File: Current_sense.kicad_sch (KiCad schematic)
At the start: 5 parts, among them U33 INA180A4

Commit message: pcb is in progress, finishing H-bridge layout
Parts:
- R64: footprint Resistor_SMD:R_2512_6332Metric -> Resistor_SMD:R_2512_6332Metric_Pad1.40x3.35mm_HandSolder
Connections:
- net INA_OUT: now reaches R65.1, U33.1 (OUT)
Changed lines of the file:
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@@
     (effects (font (size 1.27 1.27)) (justify left bottom))
+  )
+  (label "INA_OUT" (at 139.7 82.55 0)
+    (effects (font (size 0.7 0.7)) (justify left bottom))
   )
   (hierarchical_label "OUT-" (shape output) (at 104.14 90.17 270)
@@
       (effects (font (size 1.27 1.27)) (justify left))
     )
-    (property "Footprint" "Resistor_SMD:R_2512_6332Metric" (id 2) (at 102.362 82.55 90)
+    (property "Footprint" "Resistor_SMD:R_2512_6332Metric_Pad1.40x3.35mm_HandSolder" (id 2) (at 102.362 82.55 90)
       (effects (font (size 1.27 1.27)) hide)
     )

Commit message: start design power input
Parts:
- added R111, R112, R113: 8mR, Resistor_SMD:R_2512_6332Metric_Pad1.40x3.35mm_HandSolder, symbol Device:R
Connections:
- net IN+: now also R111.1
- net OUT-: now also R112.2, R113.2; no longer R64.2
- new net: R111.2, R112.1
- new net: R113.1, R64.2
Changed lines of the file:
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@@
   (junction (at 104.14 77.47) (diameter 0) (color 0 0 0 0)
   )
-  (junction (at 104.14 87.63) (diameter 0) (color 0 0 0 0)
+  (junction (at 104.14 95.25) (diameter 0) (color 0 0 0 0)
+  )
+  (junction (at 104.14 96.52) (diameter 0) (color 0 0 0 0)
   )
   (wire (pts (xy 110.49 77.47) (xy 110.49 78.74))
     (stroke (width 0) (type default) (color 0 0 0 0))
   )
-  (wire (pts (xy 104.14 87.63) (xy 110.49 87.63))
-    (stroke (width 0) (type default) (color 0 0 0 0))
-  )
   (wire (pts (xy 162.56 82.55) (xy 165.1 82.55))
     (stroke (width 0) (type default) (color 0 0 0 0))
   )
-  (wire (pts (xy 104.14 87.63) (xy 104.14 90.17))
-    (stroke (width 0) (type default) (color 0 0 0 0))
-  )
   (wire (pts (xy 104.14 78.74) (xy 104.14 77.47))
     (stroke (width 0) (type default) (color 0 0 0 0))
@@
     (stroke (width 0) (type default) (color 0 0 0 0))
   )
+  (wire (pts (xy 110.49 95.25) (xy 104.14 95.25))
+    (stroke (width 0) (type default) (color 0 0 0 0))
+  )
+  (wire (pts (xy 100.33 77.47) (xy 104.14 77.47))
+    (stroke (width 0) (type default) (color 0 0 0 0))
+  )
   (wire (pts (xy 104.14 74.93) (xy 104.14 77.47))
     (stroke (width 0) (type default) (color 0 0 0 0))
   )
-  (wire (pts (xy 104.14 86.36) (xy 104.14 87.63))
+  (wire (pts (xy 104.14 96.52) (xy 104.14 97.79))
+    (stroke (width 0) (type default) (color 0 0 0 0))
+  )
+  (wire (pts (xy 100.33 96.52) (xy 104.14 96.52))
+    (stroke (width 0) (type default) (color 0 0 0 0))
+  )
+  (wire (pts (xy 100.33 78.74) (xy 100.33 77.47))
     (stroke (width 0) (type default) (color 0 0 0 0))
   )
@@
     (stroke (width 0) (type default) (color 0 0 0 0))
   )
-  (wire (pts (xy 110.49 87.63) (xy 110.49 86.36))
+  (wire (pts (xy 104.14 93.98) (xy 104.14 95.25))
+    (stroke (width 0) (type default) (color 0 0 0 0))
+  )
+  (wire (pts (xy 110.49 86.36) (xy 110.49 95.25))
     (stroke (width 0) (type default) (color 0 0 0 0))
   )
@@
     (stroke (width 0) (type default) (color 0 0 0 0))
   )
+  (wire (pts (xy 104.14 95.25) (xy 104.14 96.52))
+    (stroke (width 0) (type default) (color 0 0 0 0))
+  )
   (wire (pts (xy 133.35 82.55) (xy 152.4 82.55))
     (stroke (width 0) (type default) (color 0 0 0 0))
@@
   )
   (wire (pts (xy 110.49 86.36) (xy 113.03 86.36))
+    (stroke (width 0) (type default) (color 0 0 0 0))
+  )
+  (wire (pts (xy 100.33 93.98) (xy 100.33 96.52))
     (stroke (width 0) (type default) (color 0 0 0 0))
   )
@@
     (effects (font (size 0.7 0.7)) (justify left bottom))
   )
-  (hierarchical_label "OUT-" (shape output) (at 104.14 90.17 270)
+  (hierarchical_label "OUT-" (shape output) (at 104.14 97.79 270)
     (effects (font (size 1.27 1.27)) (justify right))
   )
@@
     )
     (property "Datasheet" "~" (id 3) (at 162.56 92.71 0)
+      (effects (font (size 1.27 1.27)) hide)
+    )
+    (pin "1")
+    (pin "2")
+  )
+  (symbol (lib_id "Device:R") (at 100.33 90.17 0) (unit 1)
+    (in_bom yes) (on_board yes)
+    (property "Reference" "R112" (id 0) (at 95.25 88.9 0)
+      (effects (font (size 1.27 1.27)) (justify left))
+    )
+    (property "Value" "8mR" (id 1) (at 93.98 91.44 0)
+      (effects (font (size 1.27 1.27)) (justify left))
+    )
+    (property "Footprint" "Resistor_SMD:R_2512_6332Metric_Pad1.40x3.35mm_HandSolder" (id 2) (at 98.552 90.17 90)
+      (effects (font (size 1.27 1.27)) hide)
+    )
+    (property "Datasheet" "~" (id 3) (at 100.33 90.17 0)
       (effects (font (size 1.27 1.27)) hide)
     )
@@
     (pin "1")
   )
+  (symbol (lib_id "Device:R") (at 104.14 90.17 0) (unit 1)
+    (in_bom yes) (on_board yes) (fields_autoplaced)
+    (property "Reference" "R113" (id 0) (at 106.68 88.8999 0)
+      (effects (font (size 1.27 1.27)) (justify left))
+    )
+    (property "Value" "8mR" (id 1) (at 106.68 91.4399 0)
+      (effects (font (size 1.27 1.27)) (justify left))
+    )
+    (property "Footprint" "Resistor_SMD:R_2512_6332Metric_Pad1.40x3.35mm_HandSolder" (id 2) (at 102.362 90.17 90)
+      (effects (font (size 1.27 1.27)) hide)
+    )
+    (property "Datasheet" "~" (id 3) (at 104.14 90.17 0)
+      (effects (font (size 1.27 1.27)) hide)
+    )
+    (pin "1")
+    (pin "2")
+  )
   (symbol (lib_id "Device:R") (at 156.21 82.55 90) (unit 1)
     (in_bom yes) (on_board yes) (fields_autoplaced)
@@
     (pin "1")
   )
+  (symbol (lib_id "Device:R") (at 100.33 82.55 0) (unit 1)
+    (in_bom yes) (on_board yes)
+    (property "Reference" "R111" (id 0) (at 95.25 81.28 0)
+      (effects (font (size 1.27 1.27)) (justify left))
+    )
+    (property "Value" "8mR" (id 1) (at 93.98 83.82 0)
+      (effects (font (size 1.27 1.27)) (justify left))
+    )
+    (property "Footprint" "Resistor_SMD:R_2512_6332Metric_Pad1.40x3.35mm_HandSolder" (id 2) (at 98.552 82.55 90)
+      (effects (font (size 1.27 1.27)) hide)
+    )
+    (property "Datasheet" "~" (id 3) (at 100.33 82.55 0)
+      (effects (font (size 1.27 1.27)) hide)
+    )
+    (pin "1")
+    (pin "2")
+  )
   (symbol (lib_id "Device:C") (at 135.89 92.71 0) (unit 1)

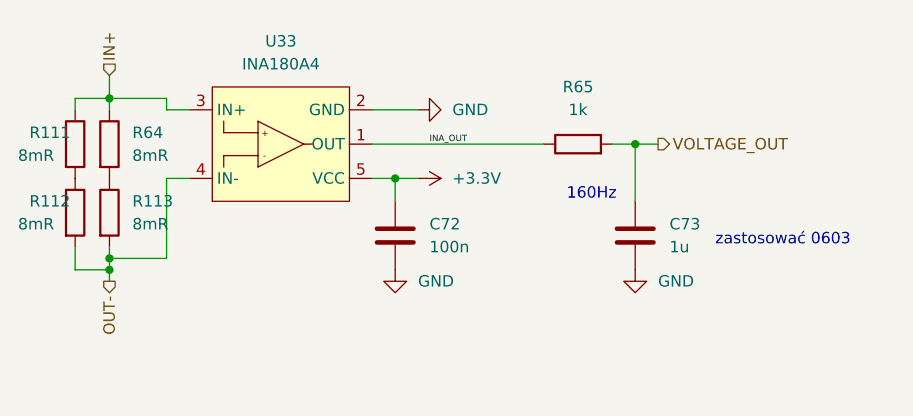
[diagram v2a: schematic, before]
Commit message: power part designed
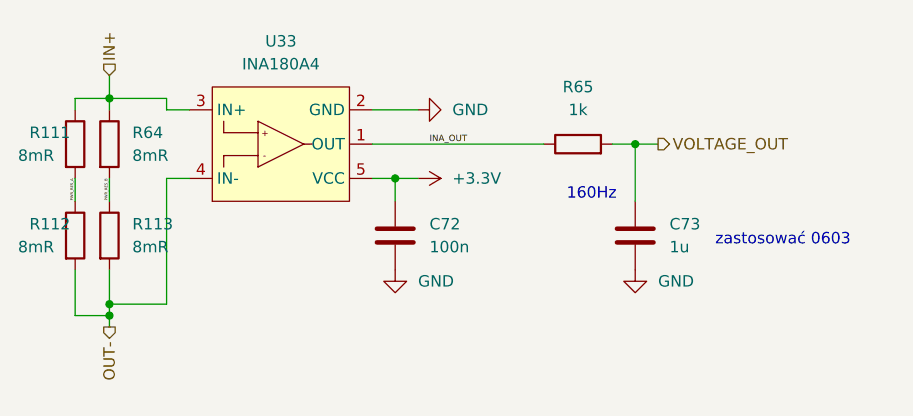
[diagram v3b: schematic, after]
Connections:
- net PWR_RES_A: now reaches R111.2, R112.1
- net PWR_RES_B: now reaches R113.1, R64.2
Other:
- moved on the sheet: R112, R113
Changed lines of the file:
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@@
   (junction (at 104.14 77.47) (diameter 0) (color 0 0 0 0)
   )
-  (junction (at 104.14 95.25) (diameter 0) (color 0 0 0 0)
-  )
-  (junction (at 104.14 96.52) (diameter 0) (color 0 0 0 0)
+  (junction (at 104.14 100.33) (diameter 0) (color 0 0 0 0)
+  )
+  (junction (at 104.14 101.6) (diameter 0) (color 0 0 0 0)
   )
   (wire (pts (xy 110.49 77.47) (xy 110.49 78.74))
@@
     (stroke (width 0) (type default) (color 0 0 0 0))
   )
+  (wire (pts (xy 104.14 96.52) (xy 104.14 100.33))
+    (stroke (width 0) (type default) (color 0 0 0 0))
+  )
   (wire (pts (xy 104.14 78.74) (xy 104.14 77.47))
     (stroke (width 0) (type default) (color 0 0 0 0))
@@
     (stroke (width 0) (type default) (color 0 0 0 0))
   )
-  (wire (pts (xy 110.49 95.25) (xy 104.14 95.25))
+  (wire (pts (xy 110.49 100.33) (xy 104.14 100.33))
+    (stroke (width 0) (type default) (color 0 0 0 0))
+  )
+  (wire (pts (xy 104.14 88.9) (xy 104.14 86.36))
     (stroke (width 0) (type default) (color 0 0 0 0))
   )
@@
     (stroke (width 0) (type default) (color 0 0 0 0))
   )
-  (wire (pts (xy 104.14 96.52) (xy 104.14 97.79))
-    (stroke (width 0) (type default) (color 0 0 0 0))
-  )
-  (wire (pts (xy 100.33 96.52) (xy 104.14 96.52))
+  (wire (pts (xy 110.49 86.36) (xy 110.49 100.33))
+    (stroke (width 0) (type default) (color 0 0 0 0))
+  )
+  (wire (pts (xy 104.14 101.6) (xy 104.14 102.87))
+    (stroke (width 0) (type default) (color 0 0 0 0))
+  )
+  (wire (pts (xy 100.33 101.6) (xy 104.14 101.6))
     (stroke (width 0) (type default) (color 0 0 0 0))
   )
@@
     (stroke (width 0) (type default) (color 0 0 0 0))
   )
-  (wire (pts (xy 104.14 93.98) (xy 104.14 95.25))
-    (stroke (width 0) (type default) (color 0 0 0 0))
-  )
-  (wire (pts (xy 110.49 86.36) (xy 110.49 95.25))
+  (wire (pts (xy 113.03 86.36) (xy 110.49 86.36))
     (stroke (width 0) (type default) (color 0 0 0 0))
   )
@@
     (stroke (width 0) (type default) (color 0 0 0 0))
   )
-  (wire (pts (xy 104.14 95.25) (xy 104.14 96.52))
+  (wire (pts (xy 104.14 100.33) (xy 104.14 101.6))
     (stroke (width 0) (type default) (color 0 0 0 0))
   )
@@
     (stroke (width 0) (type default) (color 0 0 0 0))
   )
+  (wire (pts (xy 100.33 96.52) (xy 100.33 101.6))
+    (stroke (width 0) (type default) (color 0 0 0 0))
+  )
   (wire (pts (xy 104.14 77.47) (xy 110.49 77.47))
     (stroke (width 0) (type default) (color 0 0 0 0))
@@
     (stroke (width 0) (type default) (color 0 0 0 0))
   )
-  (wire (pts (xy 110.49 86.36) (xy 113.03 86.36))
-    (stroke (width 0) (type default) (color 0 0 0 0))
-  )
-  (wire (pts (xy 100.33 93.98) (xy 100.33 96.52))
-    (stroke (width 0) (type default) (color 0 0 0 0))
-  )
   (wire (pts (xy 135.89 86.36) (xy 133.35 86.36))
+    (stroke (width 0) (type default) (color 0 0 0 0))
+  )
+  (wire (pts (xy 100.33 88.9) (xy 100.33 86.36))
     (stroke (width 0) (type default) (color 0 0 0 0))
   )
@@
     (effects (font (size 1.27 1.27)) (justify left bottom))
   )
+  (label "PWR_RES_B" (at 104.14 86.36 270)
+    (effects (font (size 0.3 0.3)) (justify right bottom))
+  )
   (label "INA_OUT" (at 139.7 82.55 0)
     (effects (font (size 0.7 0.7)) (justify left bottom))
   )
-  (hierarchical_label "OUT-" (shape output) (at 104.14 97.79 270)
+  (label "PWR_RES_A" (at 100.33 86.36 270)
+    (effects (font (size 0.3 0.3)) (justify right bottom))
+  )
+  (hierarchical_label "OUT-" (shape output) (at 104.14 102.87 270)
     (effects (font (size 1.27 1.27)) (justify right))
   )
@@
     (pin "2")
   )
-  (symbol (lib_id "Device:R") (at 100.33 90.17 0) (unit 1)
+  (symbol (lib_id "Device:R") (at 100.33 92.71 0) (unit 1)
     (in_bom yes) (on_board yes)
-    (property "Reference" "R112" (id 0) (at 95.25 88.9 0)
-      (effects (font (size 1.27 1.27)) (justify left))
-    )
-    (property "Value" "8mR" (id 1) (at 93.98 91.44 0)
-      (effects (font (size 1.27 1.27)) (justify left))
-    )
-    (property "Footprint" "Resistor_SMD:R_2512_6332Metric_Pad1.40x3.35mm_HandSolder" (id 2) (at 98.552 90.17 90)
-      (effects (font (size 1.27 1.27)) hide)
-    )
-    (property "Datasheet" "~" (id 3) (at 100.33 90.17 0)
+    (property "Reference" "R112" (id 0) (at 95.25 91.44 0)
+      (effects (font (size 1.27 1.27)) (justify left))
+    )
+    (property "Value" "8mR" (id 1) (at 93.98 93.98 0)
+      (effects (font (size 1.27 1.27)) (justify left))
+    )
+    (property "Footprint" "Resistor_SMD:R_2512_6332Metric_Pad1.40x3.35mm_HandSolder" (id 2) (at 98.552 92.71 90)
+      (effects (font (size 1.27 1.27)) hide)
+    )
+    (property "Datasheet" "~" (id 3) (at 100.33 92.71 0)
       (effects (font (size 1.27 1.27)) hide)
     )
@@
     (pin "1")
   )
-  (symbol (lib_id "Device:R") (at 104.14 90.17 0) (unit 1)
-    (in_bom yes) (on_board yes) (fields_autoplaced)
-    (property "Reference" "R113" (id 0) (at 106.68 88.8999 0)
-      (effects (font (size 1.27 1.27)) (justify left))
-    )
-    (property "Value" "8mR" (id 1) (at 106.68 91.4399 0)
-      (effects (font (size 1.27 1.27)) (justify left))
-    )
-    (property "Footprint" "Resistor_SMD:R_2512_6332Metric_Pad1.40x3.35mm_HandSolder" (id 2) (at 102.362 90.17 90)
-      (effects (font (size 1.27 1.27)) hide)
-    )
-    (property "Datasheet" "~" (id 3) (at 104.14 90.17 0)
-      (effects (font (size 1.27 1.27)) hide)
-    )
+  (symbol (lib_id "Device:R") (at 104.14 92.71 0) (unit 1)
+    (in_bom yes) (on_board yes) (fields_autoplaced)
+    (property "Reference" "R113" (id 0) (at 106.68 91.4399 0)
+      (effects (font (size 1.27 1.27)) (justify left))
+    )
+    (property "Value" "8mR" (id 1) (at 106.68 93.9799 0)
+      (effects (font (size 1.27 1.27)) (justify left))
+    )
+    (property "Footprint" "Resistor_SMD:R_2512_6332Metric_Pad1.40x3.35mm_HandSolder" (id 2) (at 102.362 92.71 90)
+      (effects (font (size 1.27 1.27)) hide)
+    )
+    (property "Datasheet" "~" (id 3) (at 104.14 92.71 0)
+      (effects (font (size 1.27 1.27)) hide)
+    )

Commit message: ADC resistors and outputs added
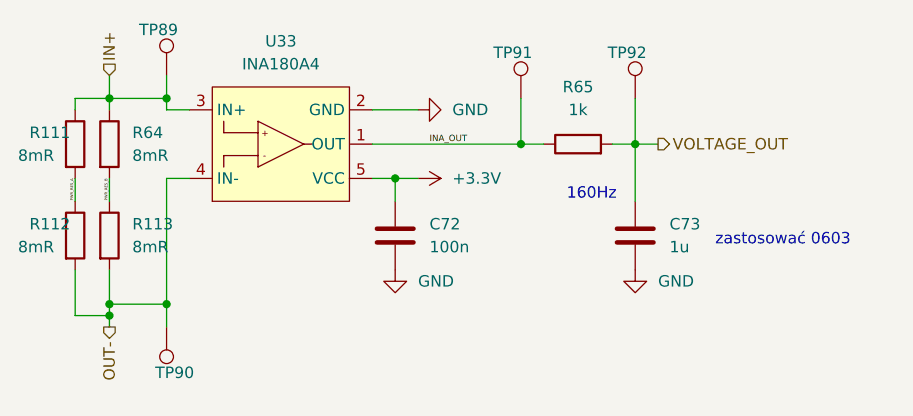
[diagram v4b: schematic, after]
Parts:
- added TP89, TP90, TP91, TP92: TestPoint, TestPoint:TestPoint_THTPad_1.0x1.0mm_Drill0.5mm, symbol Connector:TestPoint
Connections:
- net IN+: now also TP89.1
- net INA_OUT: now also TP91.1
- net OUT-: now also TP90.1
- net VOLTAGE_OUT: now also TP92.1
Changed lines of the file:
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@@
   (junction (at 135.89 86.36) (diameter 0) (color 0 0 0 0)
   )
+  (junction (at 149.86 82.55) (diameter 0) (color 0 0 0 0)
+  )
   (junction (at 104.14 77.47) (diameter 0) (color 0 0 0 0)
   )
+  (junction (at 110.49 77.47) (diameter 0) (color 0 0 0 0)
+  )
+  (junction (at 110.49 100.33) (diameter 0) (color 0 0 0 0)
+  )
   (junction (at 104.14 100.33) (diameter 0) (color 0 0 0 0)
   )
@@
     (stroke (width 0) (type default) (color 0 0 0 0))
   )
+  (wire (pts (xy 149.86 77.47) (xy 149.86 82.55))
+    (stroke (width 0) (type default) (color 0 0 0 0))
+  )
   (wire (pts (xy 162.56 82.55) (xy 165.1 82.55))
     (stroke (width 0) (type default) (color 0 0 0 0))
@@
     (stroke (width 0) (type default) (color 0 0 0 0))
   )
+  (wire (pts (xy 110.49 100.33) (xy 110.49 102.87))
+    (stroke (width 0) (type default) (color 0 0 0 0))
+  )
   (wire (pts (xy 135.89 86.36) (xy 135.89 88.9))
     (stroke (width 0) (type default) (color 0 0 0 0))
@@
     (stroke (width 0) (type default) (color 0 0 0 0))
   )
+  (wire (pts (xy 110.49 74.93) (xy 110.49 77.47))
+    (stroke (width 0) (type default) (color 0 0 0 0))
+  )
   (wire (pts (xy 100.33 101.6) (xy 104.14 101.6))
     (stroke (width 0) (type default) (color 0 0 0 0))
@@
     (stroke (width 0) (type default) (color 0 0 0 0))
   )
-  (wire (pts (xy 133.35 82.55) (xy 152.4 82.55))
+  (wire (pts (xy 133.35 82.55) (xy 149.86 82.55))
+    (stroke (width 0) (type default) (color 0 0 0 0))
+  )
+  (wire (pts (xy 149.86 82.55) (xy 152.4 82.55))
     (stroke (width 0) (type default) (color 0 0 0 0))
   )
@@
   )
   (wire (pts (xy 100.33 88.9) (xy 100.33 86.36))
+    (stroke (width 0) (type default) (color 0 0 0 0))
+  )
+  (wire (pts (xy 162.56 77.47) (xy 162.56 82.55))
     (stroke (width 0) (type default) (color 0 0 0 0))
   )
@@
     (pin "2")
   )
+  (symbol (lib_id "Connector:TestPoint") (at 149.86 77.47 0) (unit 1)
+    (in_bom yes) (on_board yes)
+    (property "Reference" "TP91" (id 0) (at 151.13 72.39 0)
+      (effects (font (size 1.27 1.27)) (justify right))
+    )
+    (property "Value" "TestPoint" (id 1) (at 147.32 72.8981 0)
+      (effects (font (size 1.27 1.27)) (justify right) hide)
+    )
+    (property "Footprint" "TestPoint:TestPoint_THTPad_1.0x1.0mm_Drill0.5mm" (id 2) (at 154.94 77.47 0)
+      (effects (font (size 1.27 1.27)) hide)
+    )
+    (property "Datasheet" "~" (id 3) (at 154.94 77.47 0)
+      (effects (font (size 1.27 1.27)) hide)
+    )
+    (pin "1")
+  )
   (symbol (lib_id "Device:R") (at 100.33 92.71 0) (unit 1)
     (in_bom yes) (on_board yes)
@@
     (pin "1")
     (pin "2")
+  )
+  (symbol (lib_id "Connector:TestPoint") (at 110.49 74.93 0) (unit 1)
+    (in_bom yes) (on_board yes)
+    (property "Reference" "TP89" (id 0) (at 111.76 69.85 0)
+      (effects (font (size 1.27 1.27)) (justify right))
+    )
+    (property "Value" "TestPoint" (id 1) (at 107.95 70.3581 0)
+      (effects (font (size 1.27 1.27)) (justify right) hide)
+    )
+    (property "Footprint" "TestPoint:TestPoint_THTPad_1.0x1.0mm_Drill0.5mm" (id 2) (at 115.57 74.93 0)
+      (effects (font (size 1.27 1.27)) hide)
+    )
+    (property "Datasheet" "~" (id 3) (at 115.57 74.93 0)
+      (effects (font (size 1.27 1.27)) hide)
+    )
+    (pin "1")
   )
   (symbol (lib_id "_IntegratedCircuits:INA180A4") (at 123.19 82.55 0) (mirror x) (unit 1)
@@
     (pin "2")
   )
+  (symbol (lib_id "Connector:TestPoint") (at 110.49 102.87 180) (unit 1)
+    (in_bom yes) (on_board yes)
+    (property "Reference" "TP90" (id 0) (at 109.22 107.95 0)
+      (effects (font (size 1.27 1.27)) (justify right))
+    )
+    (property "Value" "TestPoint" (id 1) (at 113.03 107.4419 0)
+      (effects (font (size 1.27 1.27)) (justify right) hide)
+    )
+    (property "Footprint" "TestPoint:TestPoint_THTPad_1.0x1.0mm_Drill0.5mm" (id 2) (at 105.41 102.87 0)
+      (effects (font (size 1.27 1.27)) hide)
+    )
+    (property "Datasheet" "~" (id 3) (at 105.41 102.87 0)
+      (effects (font (size 1.27 1.27)) hide)
+    )
+    (pin "1")
+  )
   (symbol (lib_id "power:GND") (at 135.89 96.52 0) (unit 1)
     (in_bom yes) (on_board yes) (fields_autoplaced)
@@
       (effects (font (size 1.27 1.27)) hide)
     )
+    (pin "1")
+  )
+  (symbol (lib_id "Connector:TestPoint") (at 162.56 77.47 0) (unit 1)
+    (in_bom yes) (on_board yes)
+    (property "Reference" "TP92" (id 0) (at 163.83 72.39 0)
+      (effects (font (size 1.27 1.27)) (justify right))
+    )
+    (property "Value" "TestPoint" (id 1) (at 160.02 72.8981 0)
+      (effects (font (size 1.27 1.27)) (justify right) hide)
+    )
+    (property "Footprint" "TestPoint:TestPoint_THTPad_1.0x1.0mm_Drill0.5mm" (id 2) (at 167.64 77.47 0)
+      (effects (font (size 1.27 1.27)) hide)
+    )
+    (property "Datasheet" "~" (id 3) (at 167.64 77.47 0)
+      (effects (font (size 1.27 1.27)) hide)
+    )
